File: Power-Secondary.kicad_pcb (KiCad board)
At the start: 2 copper layers, 83 x 60 mm, 34 parts, among them J1 SUPP PWR 1, J2 SUPP PWR 2, J3 DCDC SUPPLY, J4 FUSE +12V, Q1A1 SUP90P06-PCHANNEL-MOSFET, Q2B1 SUP90P06-PCHANNEL-MOSFET, U1 Opamp_Dual

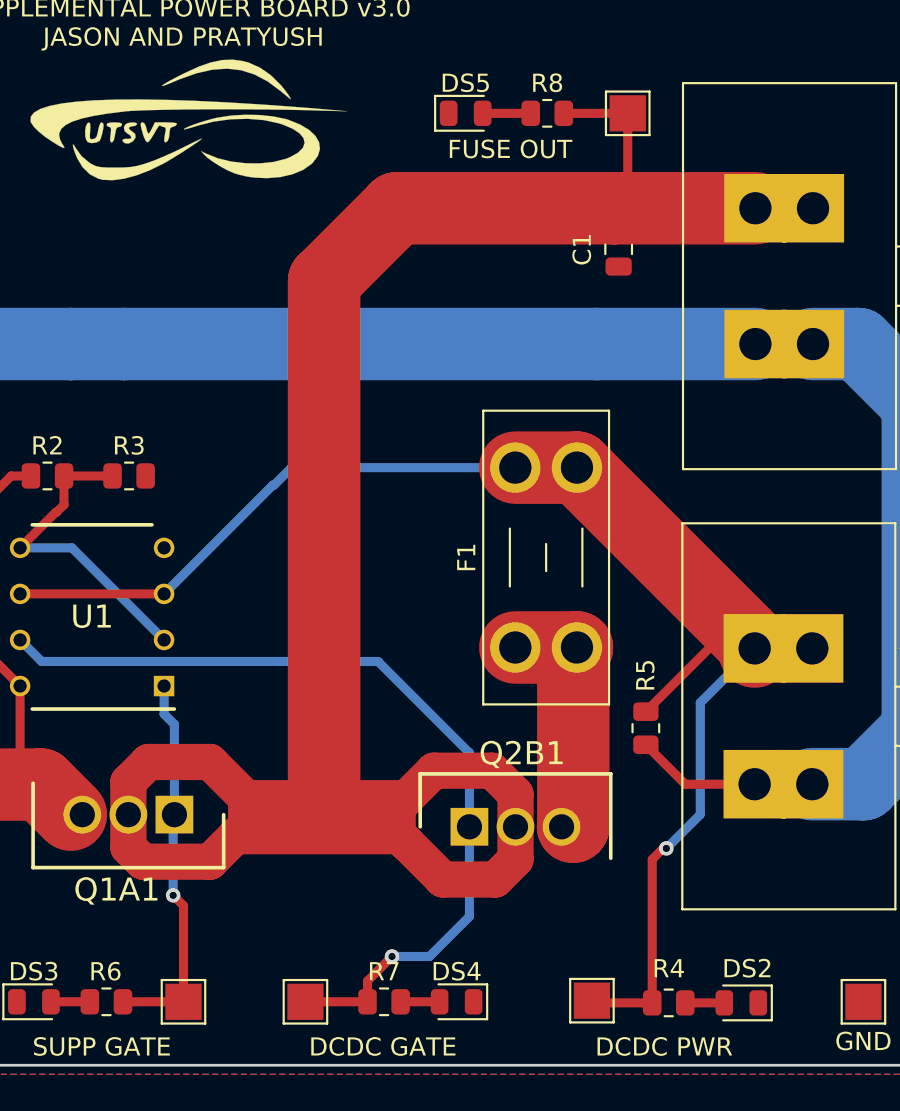
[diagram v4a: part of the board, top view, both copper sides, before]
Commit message: added planes
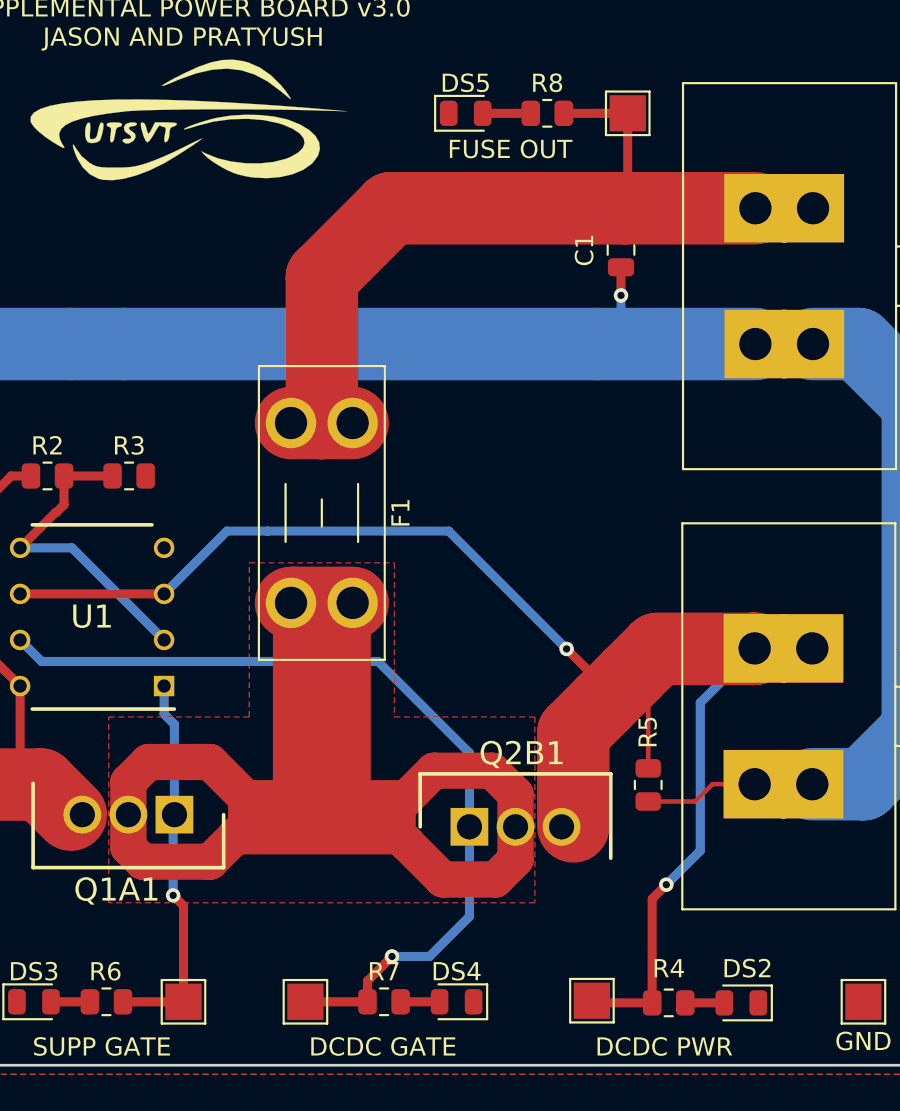
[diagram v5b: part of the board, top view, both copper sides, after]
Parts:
- moved F1 15.3 mm to (150.7, 92.0), turned to -90 degrees
- moved R5 3.13 mm to (167.0, 112.0)
- moved C1 0.14 mm to (165.5, 82.5)
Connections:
- F1 pad 1: Net-(F1-Pad1) -> FUSE_OUT
- F1 pad 2: DCDC_PWR -> Net-(F1-Pad2)
- Q1A1 pad 2: FUSE_OUT -> Net-(F1-Pad2)
- Q2B1 pad 2: FUSE_OUT -> Net-(F1-Pad2)
- Q2B1 pad 3: Net-(F1-Pad1) -> DCDC_PWR
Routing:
- net Net-(F1-Pad2): track 0.00 -> 109.1 mm
- net FUSE_OUT: track 134.2 -> 45.9 mm
- net Net-(F1-Pad1): track 14.1 -> 0.00 mm
- net DCDC_PWR: track 81.5 -> 87.5 mm, vias 1 -> 2
- net GNDS: track 120.2 -> 122.7 mm, vias 0 -> 1
- added copper zone on F.Cu, net Net-(F1-Pad2)

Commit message: gerbers and fuse
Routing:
- net GNDS: track 122.7 -> 121.4 mm
- net DCDC_PWR: track 87.5 -> 88.4 mm, vias 2 -> 1
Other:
- rule pad_to_mask_clearance: 0.2 -> 0

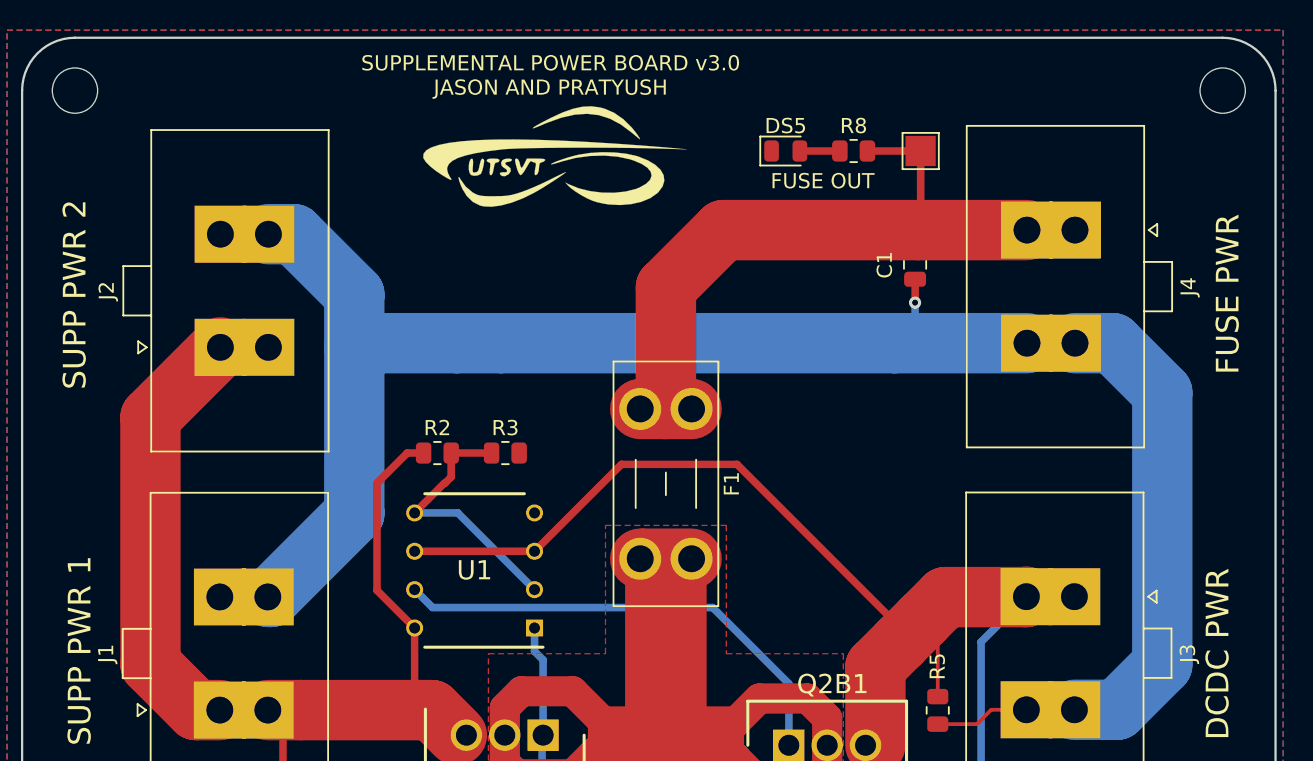
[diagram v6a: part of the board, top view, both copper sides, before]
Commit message: added supp monitor connector
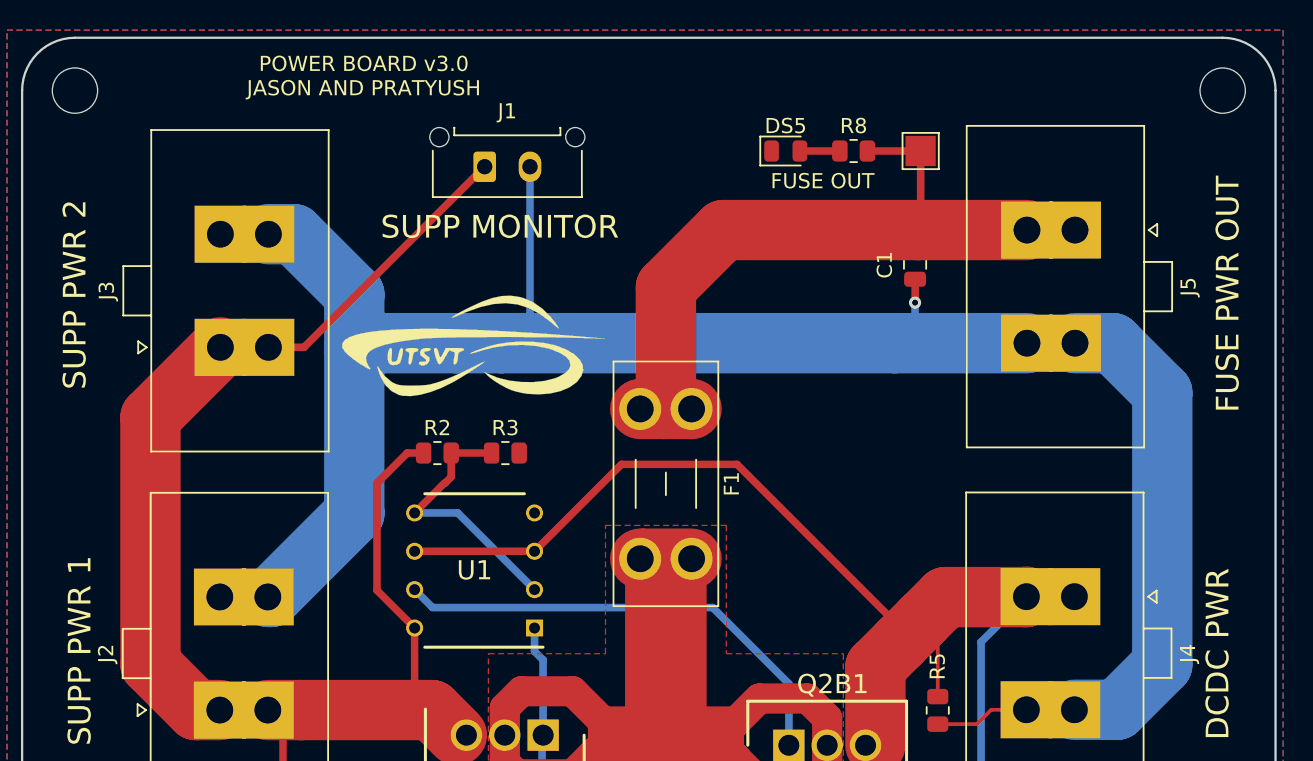
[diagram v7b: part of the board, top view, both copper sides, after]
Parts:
- added J1: SUPP PWR MON, Connector_Molex:Molex_Micro-Fit_3.0_43650-0215_1x02_P3.00mm_Vertical, F.Cu at (137.0, 76.0)
- moved LOGO1 43.6 mm to (130.0, 119.0)
- moved LOGO2 13.6 mm to (136.0, 88.0)
- renumbered J1 to J2, J2 to J3, J3 to J4, J4 to J5
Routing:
- net SUPP_PWR: track 78.1 -> 97.4 mm
- net GNDS: track 121.4 -> 133.9 mm
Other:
- board text added: "FUSE PWR OUT"
- board text added: "POWER BOARD v3.0 JASON AND PRATYUSH"
- board text added: "SUPP MONITOR"
- board text removed: "FUSE PWR"
- board text removed: "SUPPLEMENTAL POWER BOARD v3.0 JASON AND PRATYUSH"
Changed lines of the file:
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@@
     (property "Sheetname" "")
     (attr through_hole)
-    (fp_text reference "J4" (at 3.75 -10.7 90) (layer "F.SilkS")
+    (fp_text reference "J5" (at 3.75 -10.7 90) (layer "F.SilkS")
       (effects (font (size 1 1) (thickness 0.15)))
     )
@@
     (property "Sheetname" "")
     (attr through_hole)
-    (fp_text reference "J1" (at 3.75 -10.7 90) (layer "F.SilkS")
+    (fp_text reference "J2" (at 3.75 -10.7 90) (layer "F.SilkS")
       (effects (font (size 1 1) (thickness 0.15)))
     )
@@
     (property "Sheetname" "")
     (attr through_hole)
-    (fp_text reference "J3" (at 3.75 -10.7 90) (layer "F.SilkS")
+    (fp_text reference "J4" (at 3.75 -10.7 90) (layer "F.SilkS")
       (effects (font (size 1 1) (thickness 0.15)))
     )
@@
     )
   )
+  (footprint "Connector_Molex:Molex_Micro-Fit_3.0_43650-0215_1x02_P3.00mm_Vertical" (layer "F.Cu")
+    (at 137 76)
+    (descr "Molex Micro-Fit 3.0 Connector System, 43650-0215 (compatible alternatives: 43650-0216, 43650-0217), 2 Pins per row (http://www.molex.com/pdm_docs/sd/436500215_sd.pdf), generated with kicad-footprint-generator")
+    (tags "connector Molex Micro-Fit_3.0 vertical")
+    (property "Sheetfile" "Power-Secondary.kicad_sch")
+    (property "Sheetname" "")
+    (attr through_hole)
+    (fp_text reference "J1" (at 1.5 -3.67) (layer "F.SilkS")
+      (effects (font (size 1 1) (thickness 0.15)))
+    )
+    (fp_text value "SUPP PWR MON" (at 1.5 4.5) (layer "F.Fab")
+      (effects (font (size 1 1) (thickness 0.15)))
+    )
+    (fp_text user "${REFERENCE}" (at 1.5 1.2) (layer "F.Fab")
+      (effects (font (size 1 1) (thickness 0.15)))
+    )
+    (fp_line (start 6.435 2.01) (end 6.435 -1.065) (layer "F.SilkS") (width 0.12))
+    (fp_line (start 5.015 -2.58) (end 4.995 -2.58) (layer "F.SilkS") (width 0.12))
+    (fp_line (start 5.015 -2.08) (end 5.015 -2.58) (layer "F.SilkS") (width 0.12))
+    (fp_line (start -2.015 -2.08) (end 5.015 -2.08) (layer "F.SilkS") (width 0.12))
+    (fp_line (start -2.015 -2.58) (end -2.015 -2.08) (layer "F.SilkS") (width 0.12))
+    (fp_line (start -3.435 -1.065) (end -3.435 2.01) (layer "F.SilkS") (width 0.12))
+    (fp_line (start -1.995 -2.58) (end -2.015 -2.58) (layer "F.SilkS") (width 0.12))
+    (fp_line (start -3.435 2.01) (end 6.435 2.01) (layer "F.SilkS") (width 0.12))
+    (fp_line (start -3.82 -2.97) (end 6.82 -2.97) (layer "F.CrtYd") (width 0.05))
+    (fp_line (start -3.82 3.8) (end -3.82 -2.97) (layer "F.CrtYd") (width 0.05))
+    (fp_line (start 6.82 -2.97) (end 6.82 3.8) (layer "F.CrtYd") (width 0.05))
+    (fp_line (start 6.82 3.8) (end -3.82 3.8) (layer "F.CrtYd") (width 0.05))
+    (fp_line (start -3.325 -1.34) (end -2.125 -1.97) (layer "F.Fab") (width 0.1))
+    (fp_line (start -2.125 -1.97) (end -2.125 -2.47) (layer "F.Fab") (width 0.1))
+    (fp_line (start 0 -1.262893) (end 0.5 -1.97) (layer "F.Fab") (width 0.1))
+    (fp_line (start 6.325 -1.34) (end 5.125 -1.97) (layer "F.Fab") (width 0.1))
+    (fp_line (start 2.2 3.3) (end 2.2 1.9) (layer "F.Fab") (width 0.1))
+    (fp_line (start -3.325 1.9) (end 6.325 1.9) (layer "F.Fab") (width 0.1))
+    (fp_line (start 0.8 3.3) (end 2.2 3.3) (layer "F.Fab") (width 0.1))
+    (fp_line (start 5.125 -1.97) (end -2.125 -1.97) (layer "F.Fab") (width 0.1))
+    (fp_line (start 6.325 -2.47) (end 5.125 -2.47) (layer "F.Fab") (width 0.1))
+    (fp_line (start 0.8 1.9) (end 0.8 3.3) (layer "F.Fab") (width 0.1))
+    (fp_line (start -0.5 -1.97) (end 0 -1.262893) (layer "F.Fab") (width 0.1))
+    (fp_line (start 6.325 1.9) (end 6.325 -2.47) (layer "F.Fab") (width 0.1))
+    (fp_line (start -3.325 -2.47) (end -3.325 1.9) (layer "F.Fab") (width 0.1))
+    (fp_line (start 5.125 -2.47) (end 5.125 -1.97) (layer "F.Fab") (width 0.1))
+    (fp_line (start -2.125 -2.47) (end -3.325 -2.47) (layer "F.Fab") (width 0.1))
+    (pad "" np_thru_hole circle (at -3 -1.96) (size 1.27 1.27) (drill 1.27) (layers *.Cu *.Mask))
+    (pad "" np_thru_hole circle (at 6 -1.96) (size 1.27 1.27) (drill 1.27) (layers *.Cu *.Mask))
+    (pad "1" thru_hole roundrect (at 0 0) (size 1.5 2.02) (drill 1.02) (layers *.Cu *.Mask) (roundrect_rratio 0.166667)
+      (net 8 "SUPP_PWR") (pinfunction "Pin_1") (pintype "passive"))
+    (pad "2" thru_hole oval (at 3 0) (size 1.5 2.02) (drill 1.02) (layers *.Cu *.Mask)
+      (net 2 "GNDS") (pinfunction "Pin_2") (pintype "passive"))
+    (model "${KICAD6_3DMODEL_DIR}/Connector_Molex.3dshapes/Molex_Micro-Fit_3.0_43650-0215_1x02_P3.00mm_Vertical.wrl"
+      (offset (xyz 0 0 0))
+      (scale (xyz 1 1 1))
+      (rotate (xyz 0 0 0))
+    )
+  )
   (footprint "TestPoint:TestPoint_Pad_2.0x2.0mm" (layer "F.Cu")
     (at 178.87 123.96)
@@
   )
   (footprint "UTSVT_Special:UTSVT_Logo_Symbol" (layer "F.Cu")
-    (at 141.37 75.46)
+    (at 136 88)
     (property "Sheetfile" "Power-Secondary.kicad_sch")
     (property "Sheetname" "")
@@
     (property "Sheetname" "")
     (attr through_hole)
-    (fp_text reference "J2" (at 3.75 -10.7 90) (layer "F.SilkS")
+    (fp_text reference "J3" (at 3.75 -10.7 90) (layer "F.SilkS")
       (effects (font (size 1 1) (thickness 0.15)))
     )
@@
   )
   (footprint "UTSVT_Special:Hallock_Image_Tiny" (layer "B.Cu")
-    (at 132.87 75.46 180)
+    (at 130 119 180)
     (property "Sheetfile" "Power-Secondary.kicad_sch")
     (property "Sheetname" "")
@@
   (gr_arc (start 109.87 127.46) (mid 107.395126 126.434874) (end 106.37 123.96) (layer "Edge.Cuts") (width 0.15))
   (gr_arc (start 106.37 70.96) (mid 107.395126 68.485126) (end 109.87 67.46) (layer "Edge.Cuts") (width 0.15))
-  (gr_text "{dblquote}Rabid{dblquote}, not rabbit." (at 143.37 75.96) (layer "B.SilkS")
+  (gr_text "{dblquote}Rabid{dblquote}, not rabbit." (at 141 120) (layer "B.SilkS")
     (effects (font (size 1 1) (thickness 0.15)) (justify mirror))
   )
+  (gr_text "SUPP MONITOR" (at 138 80) (layer "F.SilkS")
+    (effects (font (size 1.5 1.5) (thickness 0.3)))
+  )
   (gr_text "SUPP PWR 2" (at 109.87 84.46 90) (layer "F.SilkS")
     (effects (font (size 1.5 1.5) (thickness 0.3)))
@@
     (effects (font (size 1.5 1.5) (thickness 0.3)))
   )
-  (gr_text "SUPPLEMENTAL POWER BOARD v3.0\nJASON AND PRATYUSH" (at 141.37 69.96) (layer "F.SilkS")
+  (gr_text "POWER BOARD v3.0\nJASON AND PRATYUSH" (at 129 70) (layer "F.SilkS")
     (effects (font (size 1 1) (thickness 0.15)))
   )
@@
     (effects (font (size 1 1) (thickness 0.15)))
   )
-  (gr_text "FUSE PWR" (at 186.22 84.44 90) (layer "F.SilkS")
+  (gr_text "FUSE PWR OUT" (at 186.22 84.44 90) (layer "F.SilkS")
     (effects (font (size 1.5 1.5) (thickness 0.3)))
   )
@@
   (via (at 165.5 85) (size 0.8) (drill 0.4) (layers "F.Cu" "B.Cu") (net 2))
   (segment (start 122.84 104.49) (end 122.64 104.49) (width 4) (layer "B.Cu") (net 2))
+  (segment (start 140 85.78) (end 138.095 87.685) (width 0.5) (layer "B.Cu") (net 2))
   (segment (start 128.37 84.46) (end 128.37 87.96) (width 4) (layer "B.Cu") (net 2))
   (segment (start 181.87 90.96) (end 181.87 108.96) (width 4) (layer "B.Cu") (net 2))
@@
   (segment (start 176.09 87.685) (end 178.595 87.685) (width 4) (layer "B.Cu") (net 2))
   (segment (start 128.37 87.96) (end 128.37 98.96) (width 4) (layer "B.Cu") (net 2))
+  (segment (start 140 76) (end 140 85.78) (width 0.5) (layer "B.Cu") (net 2))
   (segment (start 172.91 87.685) (end 164.145 87.685) (width 4) (layer "B.Cu") (net 2))
   (segment (start 136.37 86.46) (end 135.145 87.685) (width 0.5) (layer "B.Cu") (net 2))
@@
   (segment (start 123.645 113.185) (end 124.85 111.98) (width 0.5) (layer "F.Cu") (net 8))
   (segment (start 114.87 92.59) (end 119.5 87.96) (width 4) (layer "F.Cu") (net 8))
+  (segment (start 137 76) (end 125.04 87.96) (width 0.5) (layer "F.Cu") (net 8))
   (segment (start 129.87 96.96) (end 131.87 94.96) (width 0.5) (layer "F.Cu") (net 8))
   (segment (start 131.87 94.96) (end 132.9575 94.96) (width 0.5) (layer "F.Cu") (net 8))
   (segment (start 132.36 106.545) (end 129.87 104.055) (width 0.5) (layer "F.Cu") (net 8))
+  (segment (start 125.04 87.96) (end 122.68 87.96) (width 0.5) (layer "F.Cu") (net 8))
   (segment (start 167 111.0875) (end 167 107) (width 0.25) (layer "F.Cu") (net 9))
   (segment (start 166 106) (end 164.5 107.5) (width 4) (layer "F.Cu") (net 9))
